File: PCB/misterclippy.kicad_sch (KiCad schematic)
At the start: 23 parts, among them J1 PWR, U1 LM393

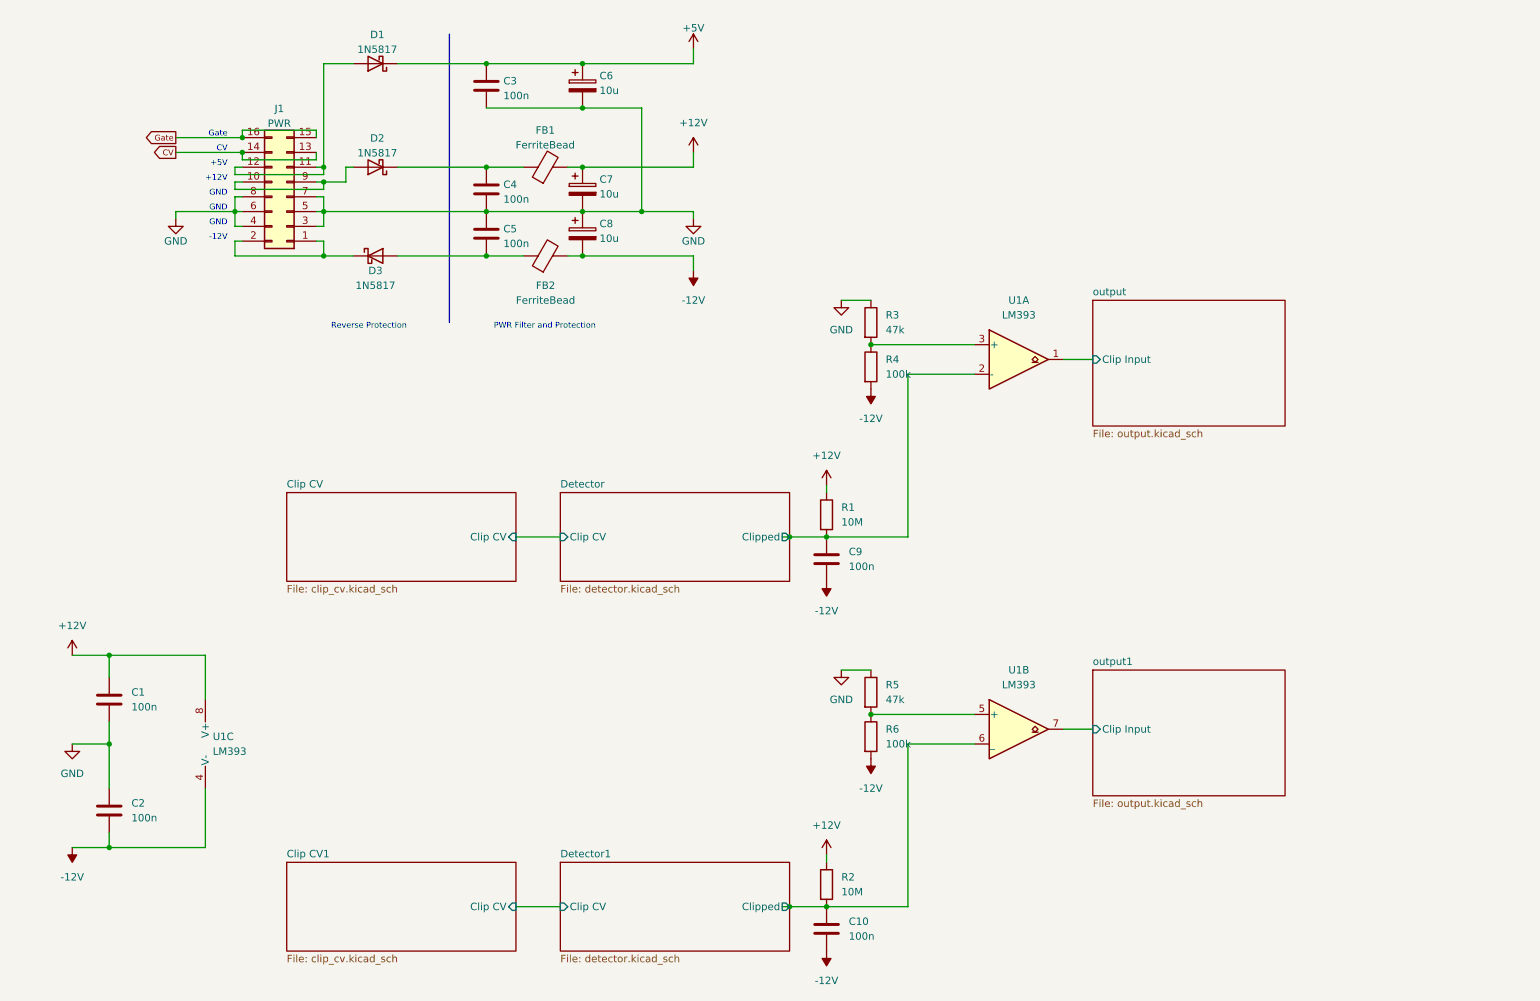
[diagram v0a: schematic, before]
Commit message: :art: Improve layout/positioning on main sheet
Also condense the voltage divider for the clip delay threshold,
as there is no load on this part and it can be shared between buffers.
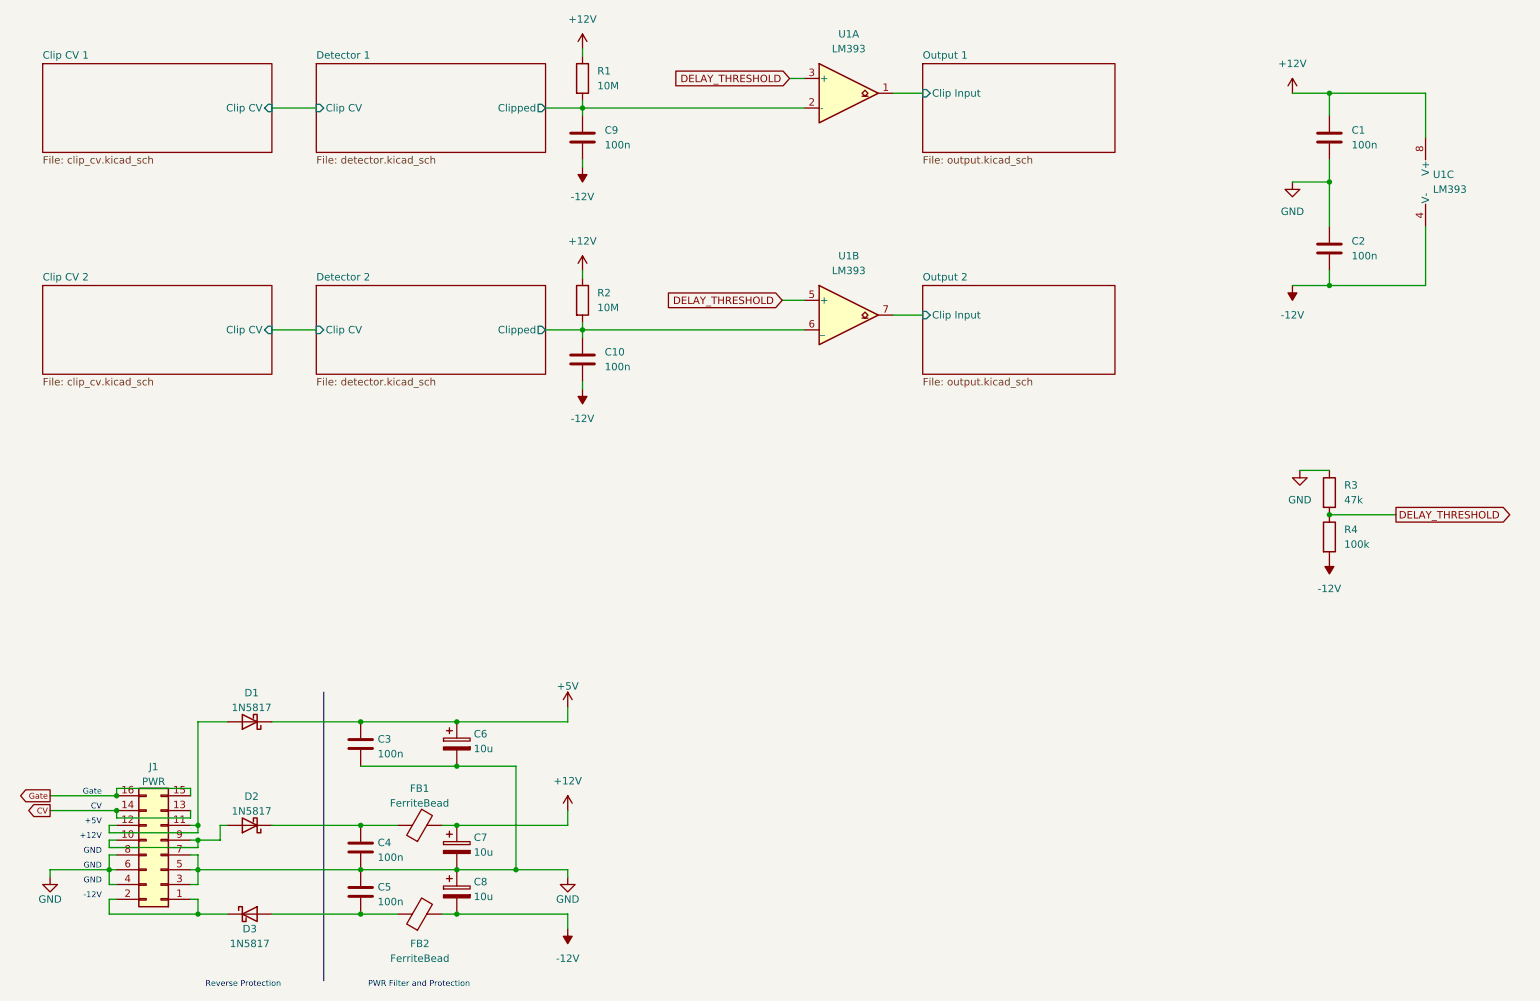
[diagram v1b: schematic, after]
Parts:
- removed R5: 47k, Resistor_THT:R_Axial_DIN0207_L6.3mm_D2.5mm_P7.62mm_Horizontal, symbol Device:R
- removed R6: 100k, Resistor_THT:R_Axial_DIN0207_L6.3mm_D2.5mm_P7.62mm_Horizontal, symbol Device:R
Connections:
- net DELAY_THRESHOLD: now reaches R3.2, R4.1, U1.3 (+)
- net DELAY_THRESHOLD: now also U1.5 (+)
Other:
- sheet Clip CV renamed Clip CV 1
- sheet Clip CV1 renamed Clip CV 2
- sheet Detector renamed Detector 1
- sheet Detector1 renamed Detector 2
- sheet output renamed Output 1
- sheet output1 renamed Output 2
- moved on the sheet: C1, C10, C2, C3, C4, C5, C6, C7, C8, C9, D1, D2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

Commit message: :wrench: Re-assign component designators
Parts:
- renumbered C3 to C1, C2 to C10, C4 to C2, C5 to C3, C6 to C4, C7 to C5, C8 to C6, C9 to C7, C10 to C8, C1 to C9

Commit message: :art: Try for a design where ICs do not cover jacks
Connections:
- net CV: no longer names the net of J1.13 (Pin_13)
- net CV: no longer J1.14 (Pin_14)
- net Gate: no longer names the net of J1.15 (Pin_15)
- net Gate: no longer J1.16 (Pin_16)
- no-connect marks 0 -> 4
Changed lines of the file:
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@@
     (rev "0")
   )
-  (junction (at 34.29 158.75) (diameter 0) (color 0 0 0 0)
-  )
   (junction (at 48.26 166.37) (diameter 0) (color 0 0 0 0)
   )
@@
   (junction (at 76.2 163.83) (diameter 0) (color 0 0 0 0)
   )
-  (junction (at 34.29 161.29) (diameter 0) (color 0 0 0 0)
-  )
+  (no_connect (at 46.99 161.29))
+  (no_connect (at 46.99 158.75))
+  (no_connect (at 34.29 161.29))
+  (no_connect (at 34.29 158.75))
   (wire (pts (xy 76.2 171.45) (xy 92.71 171.45))
     (stroke (width 0) (type default))
@@
     (stroke (width 0) (type default))
   )
-  (wire (pts (xy 22.86 161.29) (xy 34.29 161.29))
-    (stroke (width 0) (type default))
-  )
   (wire (pts (xy 242.57 53.34) (xy 242.57 60.96))
     (stroke (width 0) (type default))
@@
     (stroke (width 0) (type default))
   )
-  (wire (pts (xy 34.29 157.48) (xy 34.29 158.75))
-    (stroke (width 0) (type default))
-  )
   (wire (pts (xy 111.76 172.72) (xy 111.76 171.45))
     (stroke (width 0) (type default))
@@
     (stroke (width 0) (type default))
   )
-  (wire (pts (xy 46.99 162.56) (xy 34.29 162.56))
-    (stroke (width 0) (type default))
-  )
   (wire (pts (xy 46.99 176.53) (xy 48.26 176.53))
     (stroke (width 0) (type default))
@@
     (stroke (width 0) (type default))
   )
-  (wire (pts (xy 46.99 157.48) (xy 34.29 157.48))
-    (stroke (width 0) (type default))
-  )
-  (wire (pts (xy 34.29 161.29) (xy 34.29 162.56))
-    (stroke (width 0) (type default))
-  )
   (wire (pts (xy 33.02 165.1) (xy 48.26 165.1))
     (stroke (width 0) (type default))
@@
     (stroke (width 0) (type default))
   )
-  (wire (pts (xy 22.86 158.75) (xy 34.29 158.75))
-    (stroke (width 0) (type default))
-  )
-  (wire (pts (xy 46.99 158.75) (xy 46.99 157.48))
-    (stroke (width 0) (type default))
-  )
   (wire (pts (xy 111.76 161.29) (xy 111.76 163.83))
     (stroke (width 0) (type default))
@@
   )
   (wire (pts (xy 92.71 171.45) (xy 102.87 171.45))
-    (stroke (width 0) (type default))
-  )
-  (wire (pts (xy 46.99 161.29) (xy 46.99 162.56))
     (stroke (width 0) (type default))
   )
@@
     (effects (font (size 1 1)) (justify left bottom))
   )
-  (global_label "Gate" (shape output) (at 22.86 158.75 180) (fields_autoplaced)
-    (effects (font (size 1 1)) (justify right))
-    (property "Intersheetrefs" "${INTERSHEET_REFS}" (at -21.59 113.03 0)
-      (effects (font (size 1.27 1.27)) hide)
-    )
-    (property "Referenzen zwischen Schaltplänen" "${INTERSHEET_REFS}" (at 17.6267 158.6875 0)
-      (effects (font (size 1 1)) (justify right) hide)
-    )
-  )
-  (global_label "CV" (shape output) (at 22.86 161.29 180) (fields_autoplaced)
-    (effects (font (size 1 1)) (justify right))
-    (property "Intersheetrefs" "${INTERSHEET_REFS}" (at -21.59 113.03 0)
-      (effects (font (size 1.27 1.27)) hide)
-    )
-    (property "Referenzen zwischen Schaltplänen" "${INTERSHEET_REFS}" (at 19.1029 161.2275 0)
-      (effects (font (size 1 1)) (justify right) hide)
-    )
-  )
   (global_label "DELAY_THRESHOLD" (shape input) (at 148.59 73.66 180) (fields_autoplaced)

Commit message: fix schematics after further testing
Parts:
- R1, R2: value 10M -> 1M
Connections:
- net +12V: now also R4.2
- net -12V: no longer R4.2
- net DELAY_THRESHOLD: now also U1.2 (-), U1.6 (_); no longer U1.3 (+), U1.5 (+)
- net Detector 1/Clipped: now also U1.3 (+); no longer U1.2 (-)
- net Detector 2/Clipped: now also U1.5 (+); no longer U1.6 (_)
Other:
- moved on the sheet: R3, R4
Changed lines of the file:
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@@
   (junction (at 102.87 171.45) (diameter 0) (color 0 0 0 0)
   )
-  (junction (at 242.57 110.49) (diameter 0) (color 0 0 0 0)
+  (junction (at 242.57 116.84) (diameter 0) (color 0 0 0 0)
   )
   (junction (at 92.71 153.67) (diameter 0) (color 0 0 0 0)
@@
     (stroke (width 0) (type default))
   )
+  (wire (pts (xy 242.57 105.41) (xy 242.57 109.22))
+    (stroke (width 0) (type default))
+  )
   (wire (pts (xy 33.02 168.91) (xy 33.02 171.45))
     (stroke (width 0) (type default))
@@
     (stroke (width 0) (type default))
   )
+  (wire (pts (xy 242.57 128.27) (xy 242.57 124.46))
+    (stroke (width 0) (type default))
+  )
   (wire (pts (xy 107.95 40.64) (xy 114.3 40.64))
     (stroke (width 0) (type default))
@@
     (stroke (width 0) (type default))
   )
-  (wire (pts (xy 242.57 110.49) (xy 254 110.49))
+  (wire (pts (xy 242.57 116.84) (xy 254 116.84))
     (stroke (width 0) (type default))
   )
@@
   )
   (wire (pts (xy 92.71 179.07) (xy 111.76 179.07))
-    (stroke (width 0) (type default))
-  )
-  (wire (pts (xy 237.49 102.87) (xy 242.57 102.87))
     (stroke (width 0) (type default))
   )
@@
     )
   )
-  (global_label "DELAY_THRESHOLD" (shape output) (at 254 110.49 0) (fields_autoplaced)
+  (global_label "DELAY_THRESHOLD" (shape output) (at 254 116.84 0) (fields_autoplaced)
     (effects (font (size 1.27 1.27)) (justify left))
-    (property "Intersheetrefs" "${INTERSHEET_REFS}" (at 274.3834 110.49 0)
+    (property "Intersheetrefs" "${INTERSHEET_REFS}" (at 274.3834 116.84 0)
       (effects (font (size 1.27 1.27)) (justify left) hide)
     )
@@
     )
   )
-  (symbol (lib_id "Comparator:LM393") (at 160.02 38.1 0) (unit 1)
-    (in_bom yes) (on_board yes) (dnp no) (fields_autoplaced)
-    (property "Reference" "U1" (at 160.02 27.94 0)
-      (effects (font (size 1.27 1.27)))
-    )
-    (property "Value" "LM393" (at 160.02 30.48 0)
+  (symbol (lib_id "Comparator:LM393") (at 160.02 38.1 0) (mirror x) (unit 1)
+    (in_bom yes) (on_board yes) (dnp no)
+    (property "Reference" "U1" (at 160.02 48.26 0)
+      (effects (font (size 1.27 1.27)))
+    )
+    (property "Value" "LM393" (at 160.02 45.72 0)
       (effects (font (size 1.27 1.27)))
     )
@@
     )
   )
-  (symbol (lib_id "power:-12V") (at 242.57 118.11 0) (mirror x) (unit 1)
-    (in_bom yes) (on_board yes) (dnp no)
-    (property "Reference" "#PWR014" (at 242.57 120.65 0)
-      (effects (font (size 1.27 1.27)) hide)
-    )
-    (property "Value" "-12V" (at 242.57 123.19 0)
-      (effects (font (size 1.27 1.27)))
-    )
-    (property "Footprint" "" (at 242.57 118.11 0)
-      (effects (font (size 1.27 1.27)) hide)
-    )
-    (property "Datasheet" "" (at 242.57 118.11 0)
-      (effects (font (size 1.27 1.27)) hide)
-    )
-    (pin "1")
-    (instances
-      (project "misterclippy"
-        (path "/e63e39d7-6ac0-4ffd-8aa3-1841a4541b55"
-          (reference "#PWR014") (unit 1)
-        )
-      )
-    )
-  )
   (symbol (lib_id "power:+12V") (at 111.76 161.29 0) (unit 1)
     (in_bom yes) (on_board yes) (dnp no)
@@
   (symbol (lib_id "Device:R") (at 114.3 73.66 0) (unit 1)
     (in_bom yes) (on_board yes) (dnp no) (fields_autoplaced)
-    (property "Reference" "R2" (at 116.84 72.3899 0)
-      (effects (font (size 1.27 1.27)) (justify left))
-    )
-    (property "Value" "10M" (at 116.84 74.9299 0)
+    (property "Reference" "R2" (at 116.84 73.025 0)
+      (effects (font (size 1.27 1.27)) (justify left))
+    )
+    (property "Value" "1M" (at 116.84 75.565 0)
       (effects (font (size 1.27 1.27)) (justify left))
     )
@@
     )
   )
-  (symbol (lib_id "power:GND") (at 237.49 102.87 0) (unit 1)
-    (in_bom yes) (on_board yes) (dnp no) (fields_autoplaced)
-    (property "Reference" "#PWR013" (at 237.49 109.22 0)
-      (effects (font (size 1.27 1.27)) hide)
-    )
-    (property "Value" "GND" (at 237.49 107.95 0)
-      (effects (font (size 1.27 1.27)))
-    )
-    (property "Footprint" "" (at 237.49 102.87 0)
-      (effects (font (size 1.27 1.27)) hide)
-    )
-    (property "Datasheet" "" (at 237.49 102.87 0)
+  (symbol (lib_id "power:GND") (at 242.57 128.27 0) (mirror y) (unit 1)
+    (in_bom yes) (on_board yes) (dnp no) (fields_autoplaced)
+    (property "Reference" "#PWR013" (at 242.57 134.62 0)
+      (effects (font (size 1.27 1.27)) hide)
+    )
+    (property "Value" "GND" (at 245.11 130.175 0)
+      (effects (font (size 1.27 1.27)) (justify right))
+    )
+    (property "Footprint" "" (at 242.57 128.27 0)
+      (effects (font (size 1.27 1.27)) hide)
+    )
+    (property "Datasheet" "" (at 242.57 128.27 0)
       (effects (font (size 1.27 1.27)) hide)
     )
@@
     )
   )
-  (symbol (lib_id "Comparator:LM393") (at 160.02 76.2 0) (unit 2)
-    (in_bom yes) (on_board yes) (dnp no) (fields_autoplaced)
-    (property "Reference" "U1" (at 160.02 66.04 0)
-      (effects (font (size 1.27 1.27)))
-    )
-    (property "Value" "LM393" (at 160.02 68.58 0)
+  (symbol (lib_id "Comparator:LM393") (at 160.02 76.2 0) (mirror x) (unit 2)
+    (in_bom yes) (on_board yes) (dnp no)
+    (property "Reference" "U1" (at 160.02 86.36 0)
+      (effects (font (size 1.27 1.27)))
+    )
+    (property "Value" "LM393" (at 160.02 83.82 0)
       (effects (font (size 1.27 1.27)))
     )
@@
     )
   )
-  (symbol (lib_id "Device:R") (at 242.57 114.3 0) (unit 1)
-    (in_bom yes) (on_board yes) (dnp no) (fields_autoplaced)
-    (property "Reference" "R4" (at 245.11 113.0299 0)
-      (effects (font (size 1.27 1.27)) (justify left))
-    )
-    (property "Value" "100k" (at 245.11 115.5699 0)
-      (effects (font (size 1.27 1.27)) (justify left))
-    )
-    (property "Footprint" "Resistor_THT:R_Axial_DIN0207_L6.3mm_D2.5mm_P7.62mm_Horizontal" (at 240.792 114.3 90)
-      (effects (font (size 1.27 1.27)) hide)
-    )
-    (property "Datasheet" "~" (at 242.57 114.3 0)
+  (symbol (lib_id "Device:R") (at 242.57 113.03 0) (mirror x) (unit 1)
+    (in_bom yes) (on_board yes) (dnp no) (fields_autoplaced)
+    (property "Reference" "R4" (at 245.11 114.3001 0)
+      (effects (font (size 1.27 1.27)) (justify left))
+    )
+    (property "Value" "100k" (at 245.11 111.7601 0)
+      (effects (font (size 1.27 1.27)) (justify left))
+    )
+    (property "Footprint" "Resistor_THT:R_Axial_DIN0207_L6.3mm_D2.5mm_P7.62mm_Horizontal" (at 240.792 113.03 90)
+      (effects (font (size 1.27 1.27)) hide)
+    )
+    (property "Datasheet" "~" (at 242.57 113.03 0)
       (effects (font (size 1.27 1.27)) hide)
     )
@@
   (symbol (lib_id "Device:R") (at 114.3 35.56 0) (unit 1)
     (in_bom yes) (on_board yes) (dnp no) (fields_autoplaced)
-    (property "Reference" "R1" (at 116.84 34.2899 0)
-      (effects (font (size 1.27 1.27)) (justify left))
-    )
-    (property "Value" "10M" (at 116.84 36.8299 0)
+    (property "Reference" "R1" (at 116.84 34.925 0)
+      (effects (font (size 1.27 1.27)) (justify left))
+    )
+    (property "Value" "1M" (at 116.84 37.465 0)
       (effects (font (size 1.27 1.27)) (justify left))
     )
@@
     )
   )
+  (symbol (lib_id "power:+12V") (at 242.57 105.41 0) (unit 1)
+    (in_bom yes) (on_board yes) (dnp no) (fields_autoplaced)
+    (property "Reference" "#PWR043" (at 242.57 109.22 0)
+      (effects (font (size 1.27 1.27)) hide)
+    )
+    (property "Value" "+12V" (at 242.57 100.33 0)
+      (effects (font (size 1.27 1.27)))
+    )
+    (property "Footprint" "" (at 242.57 105.41 0)
+      (effects (font (size 1.27 1.27)) hide)
+    )
+    (property "Datasheet" "" (at 242.57 105.41 0)
+      (effects (font (size 1.27 1.27)) hide)
+    )
+    (pin "1")
+    (instances
+      (project "misterclippy"
+        (path "/e63e39d7-6ac0-4ffd-8aa3-1841a4541b55"
+          (reference "#PWR043") (unit 1)
+        )
+      )
+    )
+  )
   (symbol (lib_id "power:GND") (at 111.76 172.72 0) (unit 1)
     (in_bom yes) (on_board yes) (dnp no)
@@
     )
   )
-  (symbol (lib_id "Device:R") (at 242.57 106.68 0) (unit 1)
-    (in_bom yes) (on_board yes) (dnp no) (fields_autoplaced)
-    (property "Reference" "R3" (at 245.11 105.4099 0)
-      (effects (font (size 1.27 1.27)) (justify left))
-    )
-    (property "Value" "47k" (at 245.11 107.9499 0)
-      (effects (font (size 1.27 1.27)) (justify left))
-    )
-    (property "Footprint" "Resistor_THT:R_Axial_DIN0207_L6.3mm_D2.5mm_P7.62mm_Horizontal" (at 240.792 106.68 90)
-      (effects (font (size 1.27 1.27)) hide)
-    )
-    (property "Datasheet" "~" (at 242.57 106.68 0)
-      (effects (font (size 1.27 1.27)) hide)
-    )
+  (symbol (lib_id "Device:R") (at 242.57 120.65 0) (mirror x) (unit 1)
+    (in_bom yes) (on_board yes) (dnp no) (fields_autoplaced)
+    (property "Reference" "R3" (at 245.11 121.9201 0)
+      (effects (font (size 1.27 1.27)) (justify left))
+    )
+    (property "Value" "47k" (at 245.11 119.3801 0)
+      (effects (font (size 1.27 1.27)) (justify left))
+    )
+    (property "Footprint" "Resistor_THT:R_Axial_DIN0207_L6.3mm_D2.5mm_P7.62mm_Horizontal" (at 240.792 120.65 90)
+      (effects (font (size 1.27 1.27)) hide)
+    )
+    (property "Datasheet" "~" (at 242.57 120.65 0)
+      (effects (font (size 1.27 1.27)) hide)
+    )

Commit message: :art: Apply geographical reannotation
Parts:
- renumbered C7 to C1, C6 to C10, C5 to C11, C2 to C12, C1 to C13, C4 to C15, C9 to C2, C8 to C3, C10 to C4, C3 to C9, D2 to D3, D1 to D4, D3 to D5, FB2 to FB1, FB1 to FB2, J1 to J9, R2 to R1, R3 to R17, R4 to R18, R1 to R2
